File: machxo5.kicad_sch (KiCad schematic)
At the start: 87 parts, among them J3001 PinHeader_2x5_P1.27mm_SMD, J3002 PinHeader_2x5_P1.27mm_SMD, J3003 PinHeader_2x5_P1.27mm_SMD, J3004 PinHeader_2x5_P1.27mm_SMD, J3005 PinHeader_2x5_P1.27mm_SMD, J3006 PinHeader_2x5_P1.27mm_SMD, J3007 PinHeader_2x5_P1.27mm_SMD, J3008 PinHeader_2x5_P1.27mm_SMD, J3009 PinHeader_2x5_P1.27mm_SMD, J3010 PinHeader_2x5_P1.27mm_SMD, J3011 PinHeader_2x5_P1.27mm_SMD, SW3001 SW_KSC441J70SHLFS_SMD, SW3002 SW_KSC441J70SHLFS_SMD, SW3004 SW_KSC441J70SHLFS_SMD, Y3001 Resonator_32.768kHz_ECX-31B

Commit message: [#103910] Update power section
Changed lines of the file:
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@@
 	)
 	(bus_entry
-		(at 725.17 110.49)
-		(size 2.54 -2.54)
-		(stroke
-			(width 0)
-			(type default)
-		)
-	)
-	(bus_entry
 		(at 716.28 52.07)
 		(size -1.27 1.27)
@@
 	)
 	(bus_entry
-		(at 725.17 107.95)
-		(size 2.54 -2.54)
-		(stroke
-			(width 0)
-			(type default)
-		)
-	)
-	(bus_entry
 		(at 502.92 119.38)
 		(size 2.54 2.54)
@@
 		)
 	)
-	(bus
-		(pts
-			(xy 728.98 102.87) (xy 730.25 102.87)
-		)
-		(stroke
-			(width 0)
-			(type default)
-		)
-	)
 	(wire
 		(pts
@@
 		)
 	)
-	(bus
-		(pts
-			(xy 728.98 102.87) (xy 727.71 104.14)
-		)
-		(stroke
-			(width 0)
-			(type default)
-		)
-	)
 	(wire
 		(pts
@@
 	(wire
 		(pts
-			(xy 707.39 107.95) (xy 725.17 107.95)
-		)
-		(stroke
-			(width 0)
-			(type default)
-		)
-	)
-	(wire
-		(pts
 			(xy 755.65 114.3) (xy 764.54 114.3)
 		)
@@
 	(wire
 		(pts
-			(xy 707.39 110.49) (xy 725.17 110.49)
-		)
-		(stroke
-			(width 0)
-			(type default)
-		)
-	)
-	(wire
-		(pts
 			(xy 707.39 158.75) (xy 736.6 158.75)
 		)
@@
 		)
 	)
-	(polyline
-		(pts
-			(xy 709.168 109.22) (xy 709.168 108.712)
-		)
-		(stroke
-			(width 0)
-			(type default)
-		)
-	)
-	(polyline
-		(pts
-			(xy 708.66 106.934) (xy 709.676 106.934)
-		)
-		(stroke
-			(width 0)
-			(type default)
-		)
-	)
 	(wire
 		(pts
@@
 		)
 	)
-	(polyline
-		(pts
-			(xy 709.676 106.426) (xy 709.676 106.68)
-		)
-		(stroke
-			(width 0)
-			(type default)
-		)
-	)
 	(wire
 		(pts
@@
 		)
 	)
-	(polyline
-		(pts
-			(xy 709.168 108.712) (xy 708.66 109.22)
-		)
-		(stroke
-			(width 0)
-			(type default)
-		)
-	)
 	(wire
 		(pts
@@
 		)
 	)
-	(polyline
-		(pts
-			(xy 708.66 109.22) (xy 709.168 109.728)
-		)
-		(stroke
-			(width 0)
-			(type default)
-		)
-	)
 	(wire
 		(pts
@@
 		)
 	)
-	(bus
-		(pts
-			(xy 727.71 104.14) (xy 727.71 107.95)
-		)
-		(stroke
-			(width 0)
-			(type default)
-		)
-	)
 	(wire
 		(pts
@@
 		)
 	)
-	(polyline
-		(pts
-			(xy 710.184 106.934) (xy 709.676 106.426)
-		)
-		(stroke
-			(width 0)
-			(type default)
-		)
-	)
 	(bus
 		(pts
@@
 		)
 	)
-	(polyline
-		(pts
-			(xy 709.168 109.474) (xy 709.168 109.22)
-		)
-		(stroke
-			(width 0)
-			(type default)
-		)
-	)
 	(wire
 		(pts
@@
 		)
 	)
-	(polyline
-		(pts
-			(xy 709.676 106.68) (xy 709.676 106.934)
-		)
-		(stroke
-			(width 0)
-			(type default)
-		)
-	)
 	(wire
 		(pts
@@
 		)
 	)
-	(polyline
-		(pts
-			(xy 709.676 106.934) (xy 709.676 107.442)
-		)
-		(stroke
-			(width 0)
-			(type default)
-		)
-	)
 	(wire
 		(pts
@@
 		)
 	)
-	(polyline
-		(pts
-			(xy 709.168 109.728) (xy 709.168 109.474)
-		)
-		(stroke
-			(width 0)
-			(type default)
-		)
-	)
 	(wire
 		(pts
@@
 		)
 	)
-	(polyline
-		(pts
-			(xy 710.184 109.22) (xy 709.168 109.22)
-		)
-		(stroke
-			(width 0)
-			(type default)
-		)
-	)
 	(wire
 		(pts
@@
 		)
 	)
-	(polyline
-		(pts
-			(xy 709.676 107.442) (xy 710.184 106.934)
-		)
-		(stroke
-			(width 0)
-			(type default)
-		)
-	)
 	(wire
 		(pts
@@
 		)
 	)
-	(label "EC_UART1.TX"
-		(at 723.9 110.49 180)
-		(effects
-			(font
-				(size 1.27 1.27)
-			)
-			(justify right bottom)
-		)
-	)
 	(label "7SEG_L.E"
 		(at 510.54 132.08 0)
@@
 		)
 	)
-	(label "EC_UART1.RX"
-		(at 723.9 107.95 180)
-		(effects
-			(font
-				(size 1.27 1.27)
-			)
-			(justify right bottom)
-		)
-	)
 	(label "GPIO113"
 		(at 800.1 31.75 0)
@@
 		)
 	)
-	(hierarchical_label "EC_UART1{UART}"
-		(shape bidirectional)
-		(at 730.25 102.87 0)
-		(effects
-			(font
-				(size 1.27 1.27)
-			)
-			(justify left)
-		)
-	)
 	(hierarchical_label "EC_ESPI{eSPI}"
 		(shape bidirectional)
@@
 		)
 	)
-	(group ""
-		(members "508b201b-36a8-4669-9aba-bc3c8b2638d2" "6e736951-1751-4bda-9f5a-6b6bdd4b1eec"
-			"b5f9f712-1c48-4334-bb5e-2ac0bb87e810" "c9a7da10-2a96-4b5d-8a44-4a7360ad8d47"
-			"df42f001-1e2a-4ad6-90c2-7bee5b652b7e" "ee15e570-f132-4d68-bf2d-df49d846503e"
-		)
-	)
-	(group ""
-		(members "508908c2-79ce-4d3c-9299-027bd4fbd155" "90c8ef8e-2f62-43aa-8c62-a0e0695a5e70"
-			"932ec5f9-ec06-4538-aa9c-ae410371e162" "c7bca387-ed3e-4aa2-a90c-6cf468d304da"
-			"e03da583-7b31-4828-a13b-10393fedc08d" "e813c3f9-b9f1-43f3-bfa3-7f7be52723c4"
-		)
-	)

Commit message: [#103910] machxo5: update LFMXO5-25-7BBG400C symbol
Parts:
- removed U?: (no value), symbol antmicroFPGAChips:LFMXO5-25-7BBG400C
- added U3001: LFMXO5-25-7BBG400C, antmicro-footprints:BGA-400-17x17x0.8mm_Layout20x20_P0.8mm, symbol antmicroFPGAChips:LFMXO5-25-7BBG400C

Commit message: [#103910] machxo5: connect eSPI
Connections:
- net EC_ESPI.IO0: now also U3001.F8 (PT21B)
- net EC_ESPI.IO1: now also U3001.G9 (PT30A)
- net EC_ESPI.IO2: now also U3001.G7 (PT19A)
- net EC_ESPI.IO3: now also U3001.F9 (PT30B)
- net EC_ESPI.SCK: now also U3001.G8 (PT21A/PCLKT0_1)
- net EC_ESPI.~{ALERT0}: now also U3001.H8 (PT29A)
- net EC_ESPI.~{CS0}: now also U3001.F7 (PT19B)
- net EC_ESPI.~{RESET}: now also U3001.H9 (PT29B)
- no-connect marks 4 -> 291

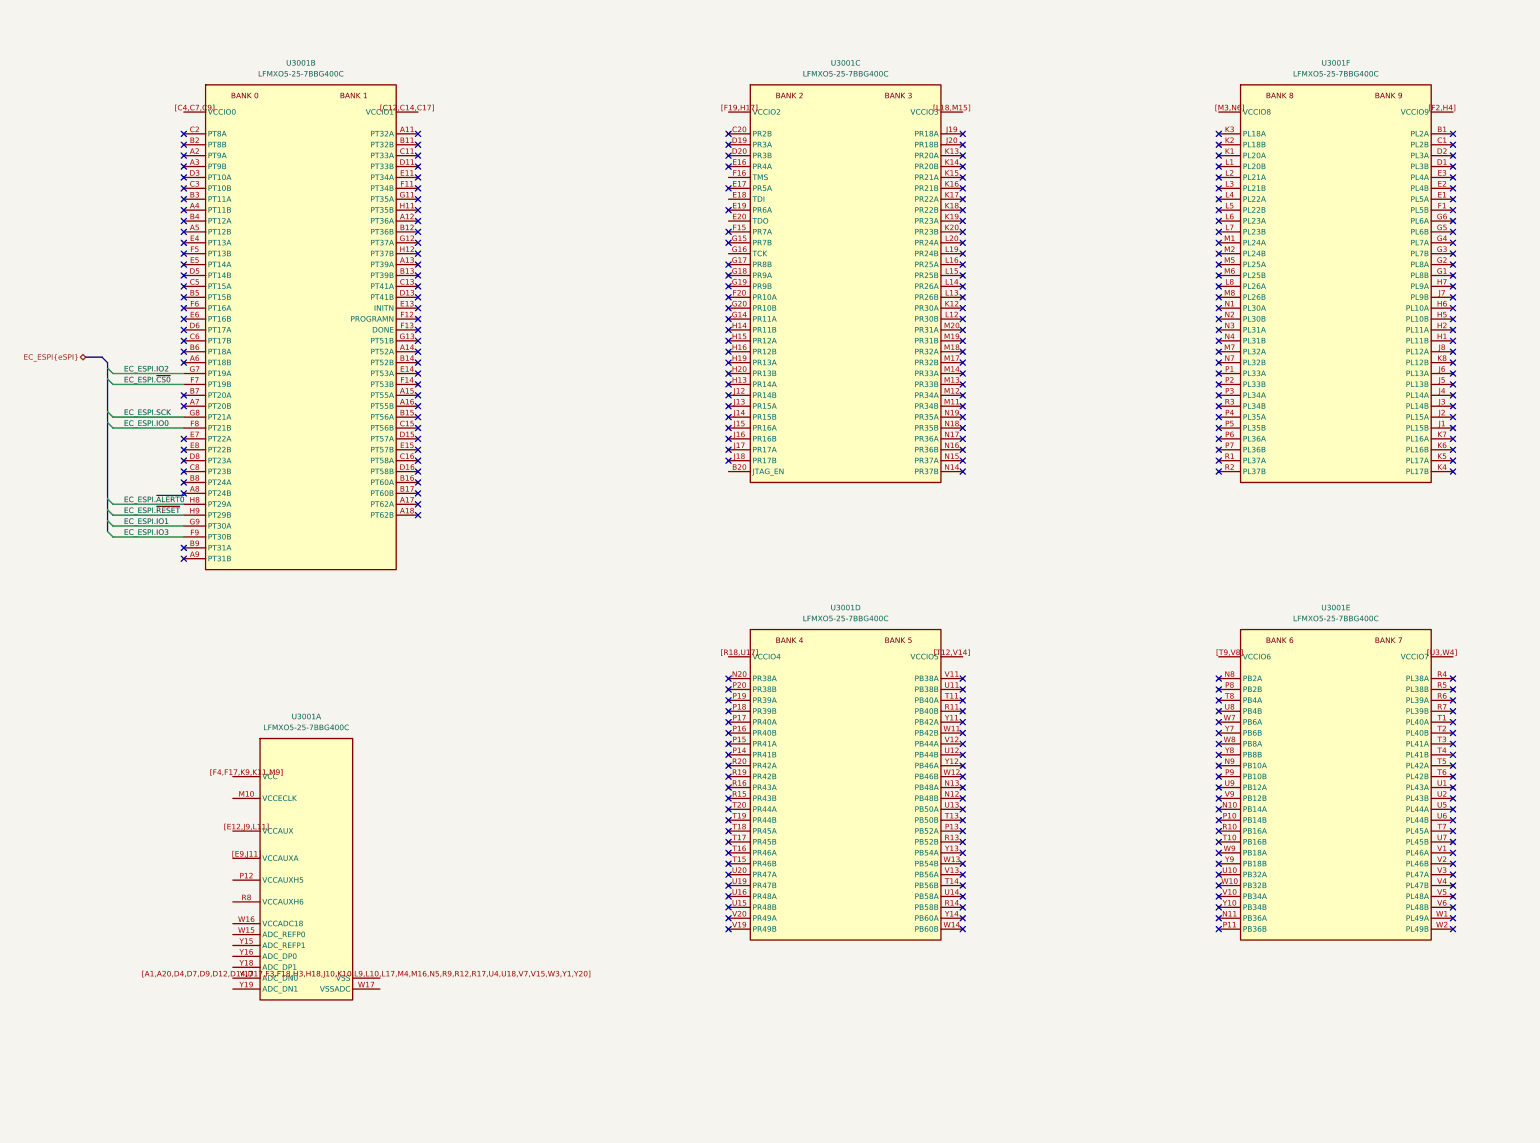
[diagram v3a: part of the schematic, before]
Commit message: [#103910] machxo5: connect JTAG, UART and LEDs
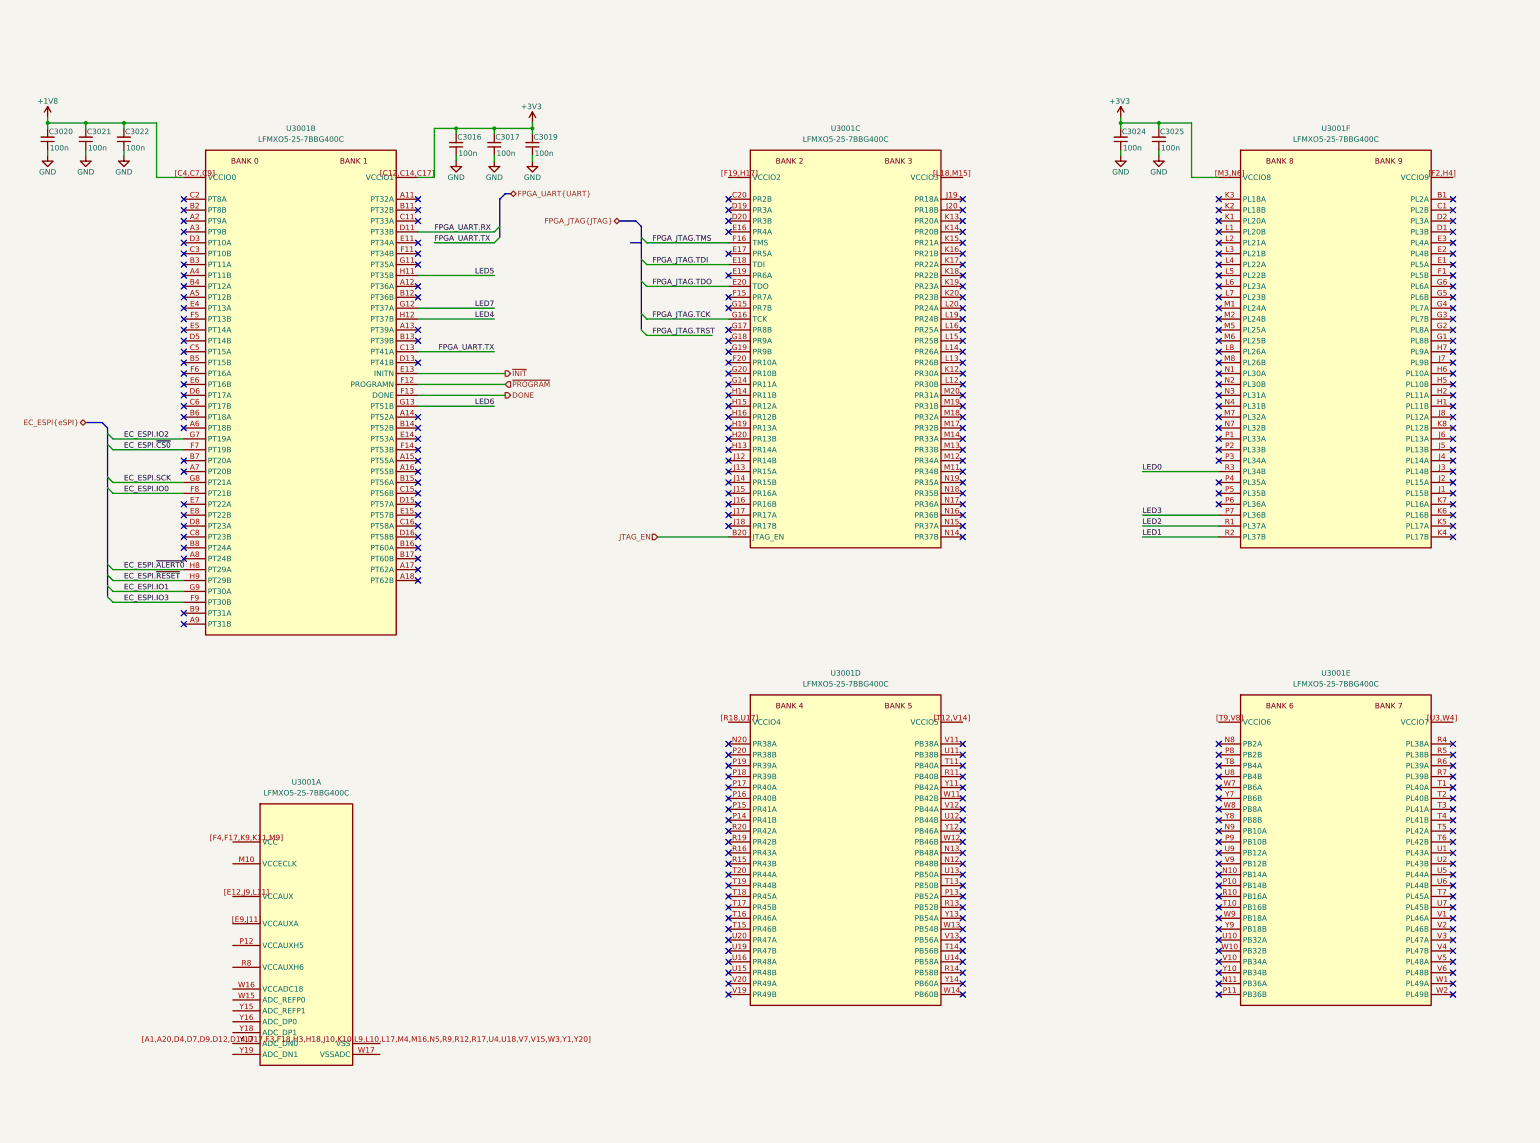
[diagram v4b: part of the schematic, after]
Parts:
- added C3016, C3017, C3019, C3020, C3021, C3022, C3024, C3025: C_100n_0402, antmicro-footprints:C_0402_1005Metric, symbol antmicroCapacitors0402:C_100n_0402
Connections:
- net +1V8: now also U3001.[C4,C7,C9] (VCCIO0), C3020.2, C3021.2, C3022.2
- net +3V3: now also U3001.[C12,C14,C17] (VCCIO1), U3001.[M3,N6] (VCCIO8), C3016.2, C3017.2, C3019.2, C3024.2, C3025.2
- net GND: now also C3016.1, C3017.1, C3019.1, C3020.1, C3021.1, C3022.1, C3024.1, C3025.1
- net LED3: now reaches U3001.P7 (PL36B)
- net LED2: now reaches U3001.R1 (PL37A/PCLKT8_1)
- net LED1: now reaches U3001.R2 (PL37B)
- net LED0: now reaches U3001.R3 (PL34B)
- net JTAG_EN: now reaches U3001.B20 (JTAG_EN)
- net FPGA_JTAG.TDI: now reaches U3001.E18 (PR5B/TDI/SSI/SD0)
- net FPGA_JTAG.TDO: now reaches U3001.E20 (PR6B/TDO/SSO/SD1)
- net FPGA_JTAG.TMS: now reaches U3001.F16 (PR4B/TMS/SCSN)
- net FPGA_JTAG.TCK: now reaches U3001.G16 (PR8A/TCK/SCLK)
- net FPGA_UART.TX: now reaches U3001.C13 (PT41A)
- net FPGA_UART.RX: now reaches U3001.D11 (PT33B)
- net ~{INIT}: now reaches U3001.E13 (PT43A/INITN)
- net ~{PROGRAM}: now reaches U3001.F12 (PT43B/PROGRAMN)
- net DONE: now reaches U3001.F13 (PT51A/DONE)
- net LED7: now reaches U3001.G12 (PT37A)
- net LED6: now reaches U3001.G13 (PT51B/MCSNO/MSDO)
- net LED5: now reaches U3001.H11 (PT35B)
- net LED4: now reaches U3001.H12 (PT37B)
- no-connect marks 291 -> 278
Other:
- moved on the sheet: U3001A, U3001B, U3001C, U3001D, U3001E, U3001F

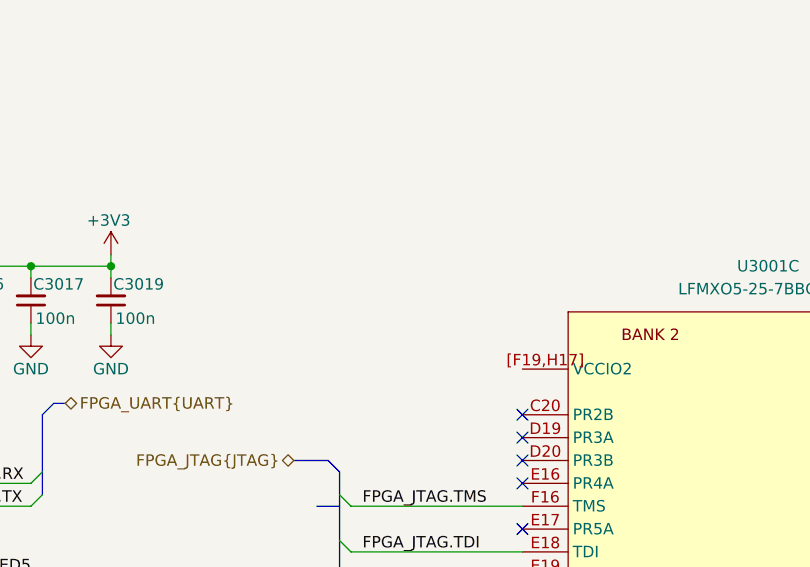
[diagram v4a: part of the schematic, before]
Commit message: [#103910] machxo5: connect 3.3V to Bank2
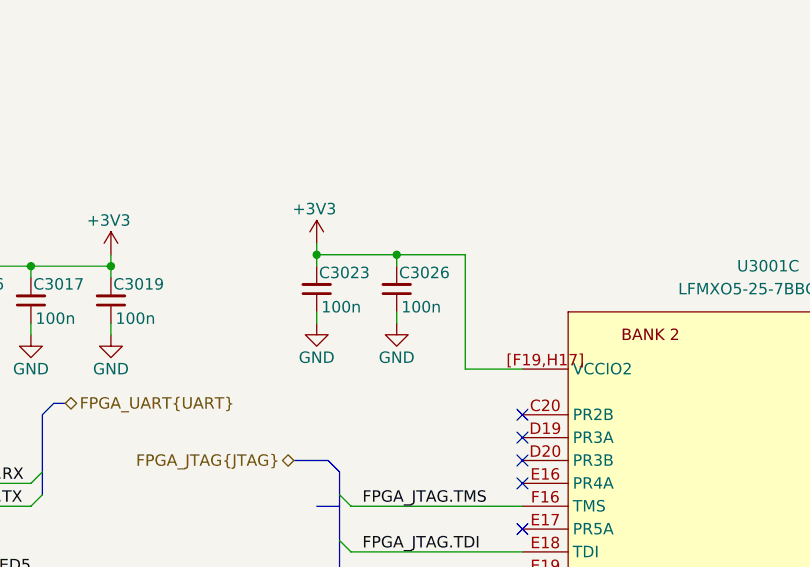
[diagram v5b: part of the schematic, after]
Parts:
- added C3023, C3026: C_100n_0402, antmicro-footprints:C_0402_1005Metric, symbol antmicroCapacitors0402:C_100n_0402
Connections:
- net +3V3: now also U3001.[F19,H17] (VCCIO2), C3023.2, C3026.2
- net GND: now also C3023.1, C3026.1
